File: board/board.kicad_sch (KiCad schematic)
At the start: 5 parts, among them J1 020_1000BASE-T_with_CT, J2 004_BASE-T_CT, U1 MagJack-A70-112-331N126

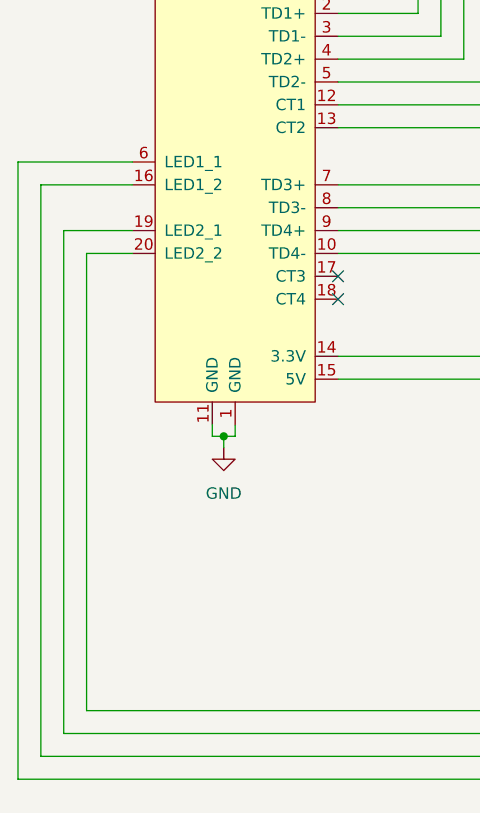
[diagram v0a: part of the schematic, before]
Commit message: led lines were backwards, fixed
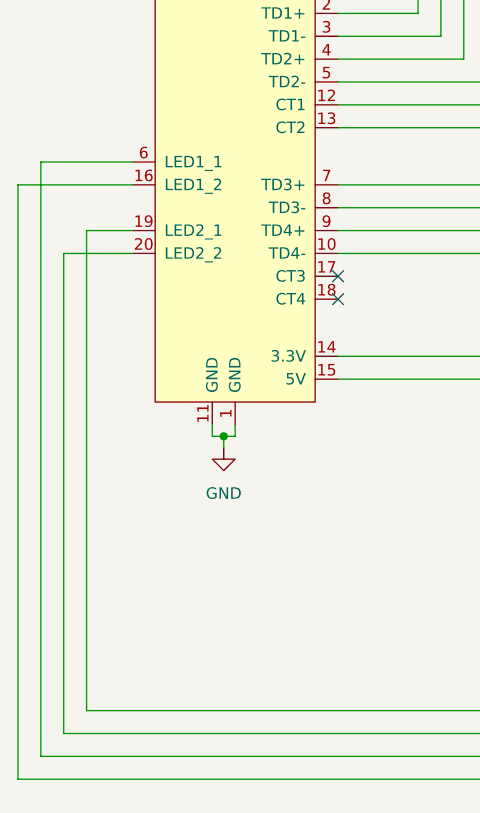
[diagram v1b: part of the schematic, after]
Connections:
- net at J1.16 (LED1_2): now also U1.18 (LEDY_K); no longer U1.17 (LEDY_A)
- net at J1.19 (LED2_1): now also U1.15 (LEDG_A); no longer U1.16 (LEDG_K)
- net at J1.20 (LED2_2): now also U1.16 (LEDG_K); no longer U1.15 (LEDG_A)
- net at J1.6 (LED1_1): now also U1.17 (LEDY_A); no longer U1.18 (LEDY_K)
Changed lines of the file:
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@@
+    (stroke (width 0) (type default) (color 0 0 0 0))
+  )
+  (wire (pts (xy 67.31 90.17) (xy 67.31 156.21))
     (stroke (width 0) (type default) (color 0 0 0 0))
   )
@@
     (stroke (width 0) (type default) (color 0 0 0 0))
   )
-  (wire (pts (xy 69.85 97.79) (xy 69.85 153.67))
-    (stroke (width 0) (type default) (color 0 0 0 0))
-  )
   (wire (pts (xy 179.07 115.57) (xy 179.07 153.67))
     (stroke (width 0) (type default) (color 0 0 0 0))
@@
   )
   (wire (pts (xy 134.62 95.25) (xy 194.31 95.25))
+    (stroke (width 0) (type default) (color 0 0 0 0))
+  )
+  (wire (pts (xy 64.77 92.71) (xy 77.47 92.71))
     (stroke (width 0) (type default) (color 0 0 0 0))
   )
@@
     (stroke (width 0) (type solid) (color 0 0 0 0))
   )
-  (wire (pts (xy 67.31 92.71) (xy 77.47 92.71))
-    (stroke (width 0) (type default) (color 0 0 0 0))
-  )
   (wire (pts (xy 127 92.71) (xy 127 82.55))
     (stroke (width 0) (type default) (color 0 0 0 0))
@@
     (stroke (width 0) (type solid) (color 0 0 0 0))
   )
-  (wire (pts (xy 64.77 90.17) (xy 77.47 90.17))
-    (stroke (width 0) (type default) (color 0 0 0 0))
-  )
-  (wire (pts (xy 69.85 97.79) (xy 77.47 97.79))
+  (wire (pts (xy 67.31 90.17) (xy 77.47 90.17))
     (stroke (width 0) (type default) (color 0 0 0 0))
   )
@@
     (stroke (width 0) (type default) (color 0 0 0 0))
   )
+  (wire (pts (xy 72.39 97.79) (xy 72.39 151.13))
+    (stroke (width 0) (type default) (color 0 0 0 0))
+  )
+  (wire (pts (xy 72.39 97.79) (xy 77.47 97.79))
+    (stroke (width 0) (type default) (color 0 0 0 0))
+  )
   (wire (pts (xy 181.61 118.11) (xy 181.61 156.21))
     (stroke (width 0) (type default) (color 0 0 0 0))
@@
     (stroke (width 0) (type default) (color 0 0 0 0))
   )
-  (wire (pts (xy 67.31 92.71) (xy 67.31 156.21))
+  (wire (pts (xy 119.38 77.47) (xy 119.38 83.82))
     (stroke (width 0) (type default) (color 0 0 0 0))
   )
-  (wire (pts (xy 64.77 90.17) (xy 64.77 158.75))
-    (stroke (width 0) (type default) (color 0 0 0 0))
-  )
-  (wire (pts (xy 119.38 77.47) (xy 119.38 83.82))
+  (wire (pts (xy 69.85 100.33) (xy 69.85 153.67))
     (stroke (width 0) (type default) (color 0 0 0 0))
   )
@@
     (stroke (width 0) (type default) (color 0 0 0 0))
   )
-  (wire (pts (xy 72.39 100.33) (xy 72.39 151.13))
-    (stroke (width 0) (type default) (color 0 0 0 0))
-  )
   (wire (pts (xy 132.08 97.79) (xy 132.08 90.17))
     (stroke (width 0) (type default) (color 0 0 0 0))
@@
     (stroke (width 0) (type default) (color 0 0 0 0))
   )
+  (wire (pts (xy 69.85 100.33) (xy 77.47 100.33))
+    (stroke (width 0) (type default) (color 0 0 0 0))
+  )
   (wire (pts (xy 100.33 73.66) (xy 109.22 73.66))
     (stroke (width 0) (type default) (color 0 0 0 0))
   )
   (wire (pts (xy 100.33 95.25) (xy 129.54 95.25))
-    (stroke (width 0) (type default) (color 0 0 0 0))
-  )
-  (wire (pts (xy 72.39 100.33) (xy 77.47 100.33))
     (stroke (width 0) (type default) (color 0 0 0 0))
   )
@@
     (stroke (width 0) (type default) (color 0 0 0 0))
   )
+  (wire (pts (xy 64.77 92.71) (xy 64.77 158.75))
+    (stroke (width 0) (type default) (color 0 0 0 0))
+  )
